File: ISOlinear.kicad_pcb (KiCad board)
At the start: 2 copper layers, 20.3 x 50.8 mm, 23 parts, among them J1 USB_C_Receptacle_USB2.0, J2 Conn_01x20, J3 Conn_01x20, U1 STM32F072CBT6, U2 PRTR5V0U2X, U3 XC6206PxxxMR-Regulator_Linear

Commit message: 1/21
Initial schematic/pcb setup, no routing and no global labels connected
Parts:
- removed J2, J3: Conn_01x20, Connector_PinHeader_2.54mm:PinHeader_1x20_P2.54mm_Vertical
- added D1: D, Diode_SMD:D_SOD-123, B.Cu at (95.4, 130.8)
- added D10: D, Diode_SMD:D_SOD-123, B.Cu at (266.9, 130.7)
- added D11: D, Diode_SMD:D_SOD-123, B.Cu at (285.9, 130.7)
- added D12: D, Diode_SMD:D_SOD-123, B.Cu at (305.0, 130.7)
- added D13: D, Diode_SMD:D_SOD-123, B.Cu at (331.2, 140.3)
- added D14: D, Diode_SMD:D_SOD-123, B.Cu at (95.4, 149.8)
- added D15: D, Diode_SMD:D_SOD-123, B.Cu at (114.5, 149.8)
- added D16: D, Diode_SMD:D_SOD-123, B.Cu at (133.5, 149.8)
- added D17: D, Diode_SMD:D_SOD-123, B.Cu at (152.6, 149.8)
- added D18: D, Diode_SMD:D_SOD-123, B.Cu at (171.6, 149.8)
- added D19: D, Diode_SMD:D_SOD-123, B.Cu at (190.7, 149.8)
- added D2: D, Diode_SMD:D_SOD-123, B.Cu at (114.5, 130.8)
- added D20: D, Diode_SMD:D_SOD-123, B.Cu at (209.7, 149.8)
- added D21: D, Diode_SMD:D_SOD-123, B.Cu at (228.8, 149.8)
- added D22: D, Diode_SMD:D_SOD-123, B.Cu at (247.8, 149.8)
- added D23: D, Diode_SMD:D_SOD-123, B.Cu at (266.9, 149.8)
- added D24: D, Diode_SMD:D_SOD-123, B.Cu at (285.9, 149.8)
- added D25: D, Diode_SMD:D_SOD-123, B.Cu at (307.3, 149.9)
- added D26: D, Diode_SMD:D_SOD-123, B.Cu at (95.4, 168.8)
- added D27: D, Diode_SMD:D_SOD-123, B.Cu at (114.5, 168.9)
- added D28: D, Diode_SMD:D_SOD-123, B.Cu at (133.5, 168.9)
- added D29: D, Diode_SMD:D_SOD-123, B.Cu at (152.6, 168.9)
- added D3: D, Diode_SMD:D_SOD-123, B.Cu at (133.5, 130.8)
- added D30: D, Diode_SMD:D_SOD-123, B.Cu at (171.6, 168.8)
- added D31: D, Diode_SMD:D_SOD-123, B.Cu at (190.7, 168.9)
- added D32: D, Diode_SMD:D_SOD-123, B.Cu at (209.7, 168.9)
- added D33: D, Diode_SMD:D_SOD-123, B.Cu at (228.8, 168.9)
- added D34: D, Diode_SMD:D_SOD-123, B.Cu at (247.8, 169.0)
- added D35: D, Diode_SMD:D_SOD-123, B.Cu at (266.9, 168.8)
- added D36: D, Diode_SMD:D_SOD-123, B.Cu at (285.9, 168.9)
- added D37: D, Diode_SMD:D_SOD-123, B.Cu at (316.9, 168.9)
- added D38: D, Diode_SMD:D_SOD-123, B.Cu at (97.8, 187.9)
- added D39: D, Diode_SMD:D_SOD-123, B.Cu at (121.6, 187.9)
- added D4: D, Diode_SMD:D_SOD-123, B.Cu at (152.6, 130.8)
- added D40: D, Diode_SMD:D_SOD-123, B.Cu at (145.4, 187.9)
- added D41: D, Diode_SMD:D_SOD-123, B.Cu at (178.8, 187.9)
- added D42: D, Diode_SMD:D_SOD-123, B.Cu at (219.2, 187.9)
- added D43: D, Diode_SMD:D_SOD-123, B.Cu at (250.2, 187.9)
- added D44: D, Diode_SMD:D_SOD-123, B.Cu at (271.6, 187.9)
- added D45: D, Diode_SMD:D_SOD-123, B.Cu at (290.7, 187.9)
- added D46: D, Diode_SMD:D_SOD-123, B.Cu at (309.7, 187.9)
- added D47: D, Diode_SMD:D_SOD-123, B.Cu at (328.8, 187.9)
- added D5: D, Diode_SMD:D_SOD-123, B.Cu at (171.6, 130.8)
- added D6: D, Diode_SMD:D_SOD-123, B.Cu at (190.7, 130.8)
- added D7: D, Diode_SMD:D_SOD-123, B.Cu at (209.7, 130.8)
- added D8: D, Diode_SMD:D_SOD-123, B.Cu at (228.8, 130.8)
- added D9: D, Diode_SMD:D_SOD-123, B.Cu at (247.8, 130.7)
- added SW1: SW_PUSH, emptystring:MXOnly-1U-Hotswap, F.Cu at (100.5, 126.8)
- added SW10: SW_PUSH, emptystring:MXOnly-1U-Hotswap, F.Cu at (271.9, 126.8)
- added SW11: SW_PUSH, emptystring:MXOnly-1U-Hotswap, F.Cu at (291.0, 126.8)
- added SW12: SW_PUSH, emptystring:MXOnly-1U-Hotswap, F.Cu at (310.0, 126.8)
- added SW13: SW_PUSH, emptystring:MXOnly-1U-Hotswap, F.Cu at (336.2, 136.3)
- added SW14: SW_PUSH, emptystring:MXOnly-1U-Hotswap, F.Cu at (100.5, 145.9)
- added SW15: SW_PUSH, emptystring:MXOnly-1U-Hotswap, F.Cu at (119.5, 145.9)
- added SW16: SW_PUSH, emptystring:MXOnly-1U-Hotswap, F.Cu at (138.6, 145.9)
- added SW17: SW_PUSH, emptystring:MXOnly-1U-Hotswap, F.Cu at (157.6, 145.9)
- added SW18: SW_PUSH, emptystring:MXOnly-1U-Hotswap, F.Cu at (176.7, 145.9)
- added SW19: SW_PUSH, emptystring:MXOnly-1U-Hotswap, F.Cu at (195.7, 145.9)
- added SW2: SW_PUSH, emptystring:MXOnly-1U-Hotswap, F.Cu at (119.5, 126.8)
- added SW20: SW_PUSH, emptystring:MXOnly-1U-Hotswap, F.Cu at (214.8, 145.9)
- added SW21: SW_PUSH, emptystring:MXOnly-1U-Hotswap, F.Cu at (233.8, 145.9)
- added SW22: SW_PUSH, emptystring:MXOnly-1U-Hotswap, F.Cu at (252.9, 145.9)
- added SW23: SW_PUSH, emptystring:MXOnly-1U-Hotswap, F.Cu at (271.9, 145.9)
- added SW24: SW_PUSH, emptystring:MXOnly-1U-Hotswap, F.Cu at (291.0, 145.9)
- added SW25: SW_PUSH, emptystring:MXOnly-1U-Hotswap, F.Cu at (312.4, 145.9)
- added SW26: SW_PUSH, emptystring:MXOnly-1U-Hotswap, F.Cu at (100.5, 164.9)
- added SW27: SW_PUSH, emptystring:MXOnly-1U-Hotswap, F.Cu at (119.5, 164.9)
- added SW28: SW_PUSH, emptystring:MXOnly-1U-Hotswap, F.Cu at (138.6, 164.9)
- added SW29: SW_PUSH, emptystring:MXOnly-1U-Hotswap, F.Cu at (157.6, 164.9)
- added SW3: SW_PUSH, emptystring:MXOnly-1U-Hotswap, F.Cu at (138.6, 126.8)
- added SW30: SW_PUSH, emptystring:MXOnly-1U-Hotswap, F.Cu at (176.7, 164.9)
- added SW31: SW_PUSH, emptystring:MXOnly-1U-Hotswap, F.Cu at (195.7, 164.9)
- added SW32: SW_PUSH, emptystring:MXOnly-1U-Hotswap, F.Cu at (214.8, 164.9)
- added SW33: SW_PUSH, emptystring:MXOnly-1U-Hotswap, F.Cu at (233.8, 164.9)
- added SW34: SW_PUSH, emptystring:MXOnly-1U-Hotswap, F.Cu at (252.9, 164.9)
- added SW35: SW_PUSH, emptystring:MXOnly-1U-Hotswap, F.Cu at (271.9, 164.9)
- added SW36: SW_PUSH, emptystring:MXOnly-1U-Hotswap, F.Cu at (291.0, 164.9)
- added SW37: SW_PUSH, emptystring:MXOnly-1U-Hotswap, F.Cu at (321.9, 164.9)
- added SW38: SW_PUSH, emptystring:MXOnly-1U-Hotswap, F.Cu at (102.9, 184.0)
- added SW39: SW_PUSH, emptystring:MXOnly-1U-Hotswap, F.Cu at (126.7, 184.0)
- added SW4: SW_PUSH, emptystring:MXOnly-1U-Hotswap, F.Cu at (157.6, 126.8)
- added SW40: SW_PUSH, emptystring:MXOnly-1U-Hotswap, F.Cu at (150.5, 184.0)
- added SW41: SW_PUSH, emptystring:MXOnly-1U-Hotswap, F.Cu at (183.8, 184.0)
- added SW42: SW_PUSH, emptystring:MXOnly-1U-Hotswap, F.Cu at (224.3, 184.0)
- added SW43: SW_PUSH, emptystring:MXOnly-1U-Hotswap, F.Cu at (255.3, 184.0)
- added SW44: SW_PUSH, emptystring:MXOnly-1U-Hotswap, F.Cu at (276.7, 184.0)
- added SW45: SW_PUSH, emptystring:MXOnly-1U-Hotswap, F.Cu at (295.8, 184.0)
- added SW46: SW_PUSH, emptystring:MXOnly-1U-Hotswap, F.Cu at (314.8, 184.0)
- added SW47: SW_PUSH, emptystring:MXOnly-1U-Hotswap, F.Cu at (333.9, 184.0)
- added SW5: SW_PUSH, emptystring:MXOnly-1U-Hotswap, F.Cu at (176.7, 126.8)
- added SW6: SW_PUSH, emptystring:MXOnly-1U-Hotswap, F.Cu at (195.7, 126.8)
- added SW7: SW_PUSH, emptystring:MXOnly-1U-Hotswap, F.Cu at (214.8, 126.8)
- added SW8: SW_PUSH, emptystring:MXOnly-1U-Hotswap, F.Cu at (233.8, 126.8)
- added SW9: SW_PUSH, emptystring:MXOnly-1U-Hotswap, F.Cu at (252.9, 126.8)
- BOOT1, C1, C10, C2, C3, C4, C5, C6, C7, C8, C9, F1, J1, R1, R2, R3, R4, RST1, U1, U2, U3: moved to B.Cu
- moved C4 82.4 mm to (79.3, 142.9)
- moved RST1 80.2 mm to (80.8, 164.2)
- moved C1 78.1 mm to (82.3, 154.9), turned to 180 degrees
- moved C7 78.1 mm to (82.3, 153.6), turned to 0 degrees
- moved R4 77.7 mm to (82.5, 157.2), turned to 180 degrees
- moved F1 76.0 mm to (83.8, 133.7), turned to 0 degrees
- moved J1 76.0 mm to (83.8, 121.4), turned to 0 degrees
- moved U1 76.0 mm to (83.8, 147.2)
- moved U2 76.0 mm to (83.8, 129.4), turned to 0 degrees
- moved R3 74.3 mm to (85.0, 157.2), turned to 180 degrees
- moved C9 73.9 mm to (85.3, 135.9)
- moved C10 72.3 mm to (86.5, 139.4), turned to 180 degrees
- moved BOOT1 72.0 mm to (86.8, 164.2)
- moved C8 72.0 mm to (86.8, 132.7)
- moved R1 72.0 mm to (86.8, 130.7), turned to 180 degrees
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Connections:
- U2 pad 2: D_N -> D-
- U2 pad 3: D_P -> D+
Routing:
- net NRST: track 56.2 -> 19.5 mm
- net /A10: track 26.3 -> 0.00 mm
- net /A9: track 23.5 -> 0.00 mm
- net D+: track 0.00 -> 22.1 mm
- net D_P: track 22.1 -> 0.00 mm
- net BOOT0: track 47.3 -> 25.6 mm
- net /F1: track 21.0 -> 0.00 mm
- net /A8: track 20.8 -> 0.00 mm
- net /A0: track 20.5 -> 0.00 mm
- net D_N: track 20.5 -> 0.00 mm
- net D-: track 0.00 -> 20.5 mm
- net /F0: track 18.3 -> 0.00 mm
- net /B15: track 18.0 -> 0.00 mm
- net /A1: track 17.8 -> 0.00 mm
- net /A13: track 16.0 -> 0.00 mm
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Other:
- board size 20.3 x 50.8 mm -> 268.3 x 73.8 mm

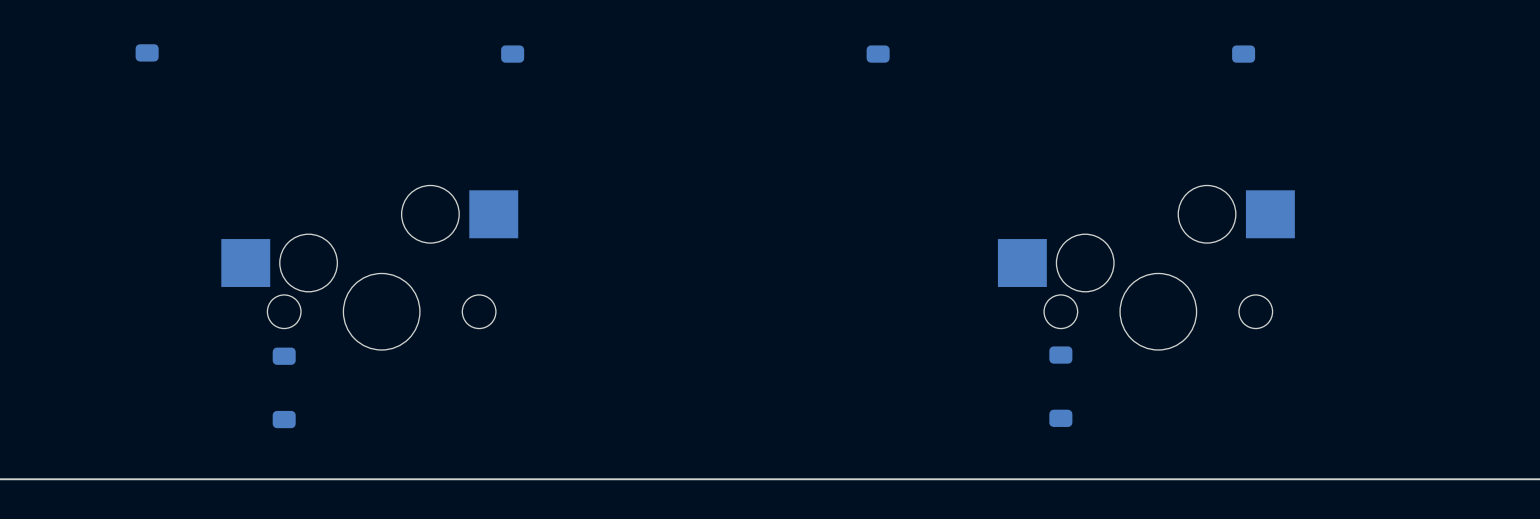
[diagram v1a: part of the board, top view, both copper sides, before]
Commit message: 1/21
Reset grid origin, placed stab footprints
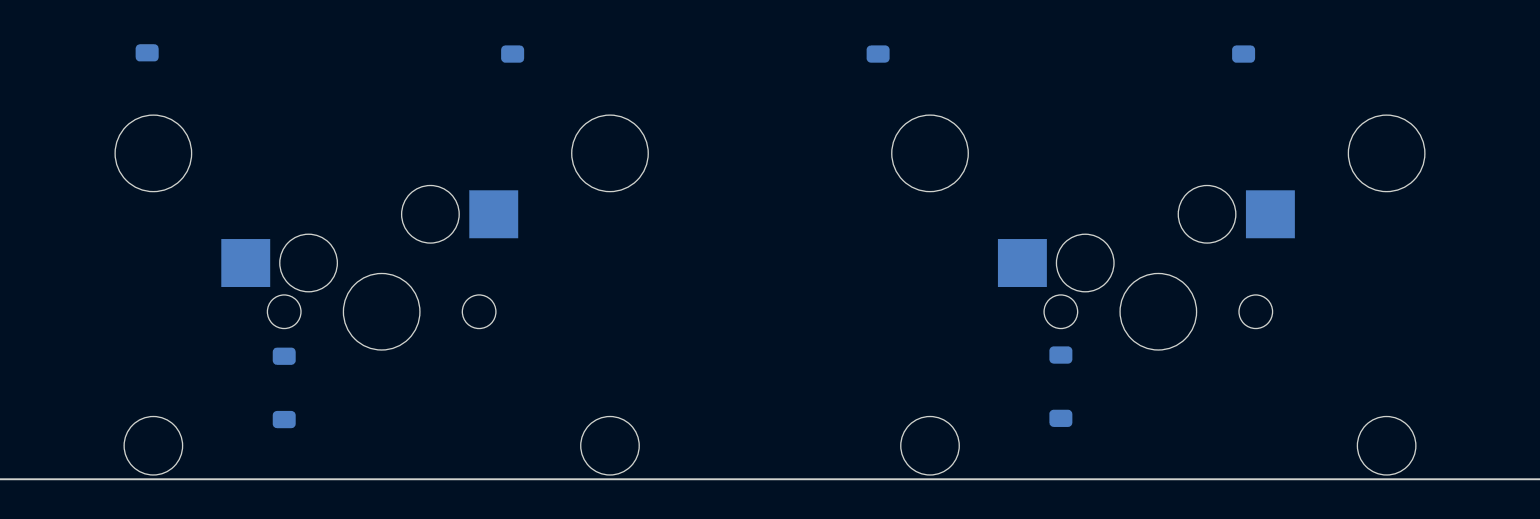
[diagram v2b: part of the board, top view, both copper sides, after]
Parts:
- added REF**: SW_Stabilizer, keyswitches:MX_Stabilizer_2u, F.Cu at (224.3, 184.0)
- added REF**: SW_Stabilizer, keyswitches:MX_Stabilizer_2u, F.Cu at (183.8, 184.0)
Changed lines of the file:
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@@
 		(allow_soldermask_bridges_in_footprints no)
 		(tenting front back)
-		(grid_origin 135.8925 91.9)
+		(grid_origin 90.96625 117.3)
 		(pcbplotparams
 			(layerselection 0x00000000_00000000_55555555_5755f5ff)
@@
 		)
 	)
+	(footprint "keyswitches:MX_Stabilizer_2u"
+		(layer "F.Cu")
+		(at 224.31625 183.975 180)
+		(descr "MX-style stabilizer mount")
+		(tags "MX,cherry,gateron,kailh,pg1511,stabilizer,stab")
+		(property "Reference" "REF**"
+			(at 0 10 0)
+			(layer "Cmts.User")
+			(hide yes)
+			(effects
+				(font
+					(size 1 1)
+					(thickness 0.15)
+				)
+			)
+		)
+		(property "Value" "SW_Stabilizer"
+			(at 0 -8.7 0)
+			(layer "F.Fab")
+			(hide yes)
+			(effects
+				(font
+					(size 1 1)
+					(thickness 0.15)
+				)
+			)
+		)
+		(property "Datasheet" ""
+			(at 0 0 0)
+			(layer "F.Fab")
+			(hide yes)
+			(effects
+				(font
+					(size 1.27 1.27)
+					(thickness 0.15)
+				)
+			)
+		)
+		(property "Description" ""
+			(at 0 0 0)
+			(layer "F.Fab")
+			(hide yes)
+			(effects
+				(font
+					(size 1.27 1.27)
+					(thickness 0.15)
+				)
+			)
+		)
+		(attr through_hole)
+		(fp_circle
+			(center 0 0)
+			(end 3 0)
+			(stroke
+				(width 0.15)
+				(type solid)
+			)
+			(fill no)
+			(layer "Cmts.User")
+		)
+		(pad "" np_thru_hole circle
+			(at -11.9 -6.985 180)
+			(size 3.048 3.048)
+			(drill 3.048)
+			(layers "*.Cu" "*.Mask")
+		)
+		(pad "" np_thru_hole circle
+			(at -11.9 8.255 180)
+			(size 3.9878 3.9878)
+			(drill 3.9878)
+			(layers "*.Cu" "*.Mask")
+		)
+		(pad "" np_thru_hole circle
+			(at 11.9 -6.985 180)
+			(size 3.048 3.048)
+			(drill 3.048)
+			(layers "*.Cu" "*.Mask")
+		)
+		(pad "" np_thru_hole circle
+			(at 11.9 8.255 180)
+			(size 3.9878 3.9878)
+			(drill 3.9878)
+			(layers "*.Cu" "*.Mask")
+		)
+		(embedded_fonts no)
+	)
 	(footprint "emptystring:MXOnly-1U-Hotswap"
 		(layer "F.Cu")
@@
 		)
 	)
+	(footprint "keyswitches:MX_Stabilizer_2u"
+		(layer "F.Cu")
+		(at 183.835 183.975 180)
+		(descr "MX-style stabilizer mount")
+		(tags "MX,cherry,gateron,kailh,pg1511,stabilizer,stab")
+		(property "Reference" "REF**"
+			(at 0 10 0)
+			(layer "Cmts.User")
+			(hide yes)
+			(effects
+				(font
+					(size 1 1)
+					(thickness 0.15)
+				)
+			)
+		)
+		(property "Value" "SW_Stabilizer"
+			(at 0 -8.7 0)
+			(layer "F.Fab")
+			(hide yes)
+			(effects
+				(font
+					(size 1 1)
+					(thickness 0.15)
+				)
+			)
+		)
+		(property "Datasheet" ""
+			(at 0 0 0)
+			(layer "F.Fab")
+			(hide yes)
+			(effects
+				(font
+					(size 1.27 1.27)
+					(thickness 0.15)
+				)
+			)
+		)
+		(property "Description" ""
+			(at 0 0 0)
+			(layer "F.Fab")
+			(hide yes)
+			(effects
+				(font
+					(size 1.27 1.27)
+					(thickness 0.15)
+				)
+			)
+		)
+		(attr through_hole)
+		(fp_circle
+			(center 0 0)
+			(end 3 0)
+			(stroke
+				(width 0.15)
+				(type solid)
+			)
+			(fill no)
+			(layer "Cmts.User")
+		)
+		(pad "" np_thru_hole circle
+			(at -11.9 -6.985 180)
+			(size 3.048 3.048)
+			(drill 3.048)
+			(layers "*.Cu" "*.Mask")
+		)
+		(pad "" np_thru_hole circle
+			(at -11.9 8.255 180)
+			(size 3.9878 3.9878)
+			(drill 3.9878)
+			(layers "*.Cu" "*.Mask")
+		)
+		(pad "" np_thru_hole circle
+			(at 11.9 -6.985 180)
+			(size 3.048 3.048)
+			(drill 3.048)
+			(layers "*.Cu" "*.Mask")
+		)
+		(pad "" np_thru_hole circle
+			(at 11.9 8.255 180)
+			(size 3.9878 3.9878)
+			(drill 3.9878)
+			(layers "*.Cu" "*.Mask")
+		)
+		(embedded_fonts no)
+	)
 	(footprint "emptystring:MXOnly-1U-Hotswap"

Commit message: 1/21
changed layout to teeth version, started routing rows and columns
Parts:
- removed the D13 at (331.2, 140.3)
- removed the D37 at (316.9, 168.9)
- removed D47: D, Diode_SMD:D_SOD-123
- removed the REF** at (224.3, 184.0)
- removed the REF** at (183.8, 184.0)
- removed the SW13 at (336.2, 136.3)
- removed the SW37 at (321.9, 164.9)
- removed SW47: SW_PUSH, emptystring:MXOnly-1U-Hotswap
- added REF**: SW_Stabilizer, keyswitches:MX_Stabilizer_2u, F.Cu at (224.3, 184.1)
- added REF**: SW_Stabilizer, keyswitches:MX_Stabilizer_2u, F.Cu at (183.8, 184.1)
- moved SW24 10.8 mm to (317.1, 155.6)
- moved D24 10.5 mm to (311.6, 159.5)
- moved SW41 7.09 mm to (262.4, 184.1)
- moved D41 6.61 mm to (256.8, 188.1)
- moved SW42 4.71 mm to (281.4, 184.1)
- moved SW44 4.71 mm to (319.5, 184.1)
- moved SW43 4.71 mm to (300.5, 184.1)
- moved D42 4.24 mm to (275.9, 188.2)
- moved D43 4.23 mm to (294.9, 188.1)
- moved D44 4.23 mm to (314.0, 188.1)
- moved SW35 2.33 mm to (293.3, 165.1)
- moved D35 1.86 mm to (287.8, 169.1)
- moved D12 0.58 mm to (304.4, 131.0)
- moved D17 0.58 mm to (171.1, 150.0)
- moved D29 0.58 mm to (171.1, 169.1)
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- renumbered D14 to D13, D15 to D14, D16 to D15, D17 to D16, D18 to D17, D19 to D18, D20 to D19, D21 to D20, D22 to D21, D23 to D22, D24 to D23, D25 to D24, D26 to D25, D27 to D26, D28 to D27, D29 to D28, D30 to D29, D31 to D30, D32 to D31, D33 to D32, D34 to D33, D35 to D34, D36 to D35, D38 to D36, D39 to D37, D40 to D38, D41 to D39, D42 to D40, D43 to D41, D44 to D42, D45 to D43, D46 to D44, SW14 to SW13, SW15 to SW14, SW16 to SW15, SW17 to SW16, SW18 to SW17, SW19 to SW18, SW20 to SW19, SW21 to SW20, SW22 to SW21, SW23 to SW22, SW24 to SW23, SW25 to SW24, SW26 to SW25, SW27 to SW26, SW28 to SW27, SW29 to SW28, SW30 to SW29, SW31 to SW30, SW32 to SW31, SW33 to SW32, SW34 to SW33, SW35 to SW34, SW36 to SW35, SW38 to SW36, SW39 to SW37, SW40 to SW38, SW41 to SW39, SW42 to SW40, SW43 to SW41, SW44 to SW42, SW45 to SW43, SW46 to SW44
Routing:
- net ROW1: track 0.00 -> 220.6 mm
- net ROW3: track 0.00 -> 218.0 mm
- net ROW0: track 0.00 -> 209.5 mm
- net ROW2: track 0.00 -> 192.9 mm
- net Net-(D12-A): track 0.00 -> 5.49 mm
- net Net-(D11-A): track 0.00 -> 5.49 mm
- net Net-(D10-A): track 0.00 -> 5.49 mm
- net Net-(D23-A): track 0.00 -> 5.49 mm
- net Net-(D22-A): track 0.00 -> 5.49 mm
- net Net-(D21-A): track 0.00 -> 5.49 mm
- net Net-(D24-A): track 0.00 -> 5.43 mm
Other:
- board size 268.3 x 73.8 mm -> 253.2 x 73 mm

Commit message: 1/21
Matrix routing done
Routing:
- net COL2: track 0.00 -> 72.7 mm, vias 0 -> 6
- net COL9: track 0.00 -> 70.4 mm, vias 0 -> 6
- net COL6: track 0.00 -> 70.4 mm, vias 0 -> 6
- net COL8: track 0.00 -> 70.3 mm, vias 0 -> 6
- net COL1: track 0.00 -> 68.0 mm, vias 0 -> 6
- net COL4: track 0.00 -> 68.0 mm, vias 0 -> 6
- net COL10: track 0.00 -> 67.1 mm, vias 0 -> 4
- net COL0: track 0.00 -> 64.2 mm, vias 0 -> 6
- net COL11: track 0.00 -> 61.1 mm
- net COL5: track 0.00 -> 42.9 mm, vias 0 -> 4
- net COL7: track 0.00 -> 42.9 mm, vias 0 -> 4
- net COL3: track 0.00 -> 42.8 mm, vias 0 -> 4
- net Net-(D35-A): track 0.00 -> 5.55 mm
- net Net-(D32-A): track 0.00 -> 5.55 mm
- net Net-(D42-A): track 0.00 -> 5.55 mm
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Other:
- outline, holes or cut-outs redrawn

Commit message: 1/22
Routing solutions brainstorm
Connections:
- U1 pad 38: /A15 -> ROW0

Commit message: 1/23
routed and filled tentatively, no grounds on some pins
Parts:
- moved BOOT1 76.5 mm to (135.4, 105.1), turned to 0 degrees
- moved RST1 76.2 mm to (135.4, 111.1), turned to 180 degrees
- moved R3 66.4 mm to (128.4, 106.8), turned to -90 degrees
- moved R4 66.3 mm to (128.4, 109.3), turned to -90 degrees
- moved C1 63.1 mm to (126.1, 109.6), turned to -90 degrees
- moved C7 61.3 mm to (124.9, 109.6), turned to 90 degrees
- moved C6 60.9 mm to (124.1, 104.1), turned to 90 degrees
- moved C5 58.9 mm to (122.6, 103.6), turned to 0 degrees
- moved U1 52.2 mm to (118.4, 108.1), turned to 180 degrees
- moved C3 46.7 mm to (113.9, 103.8), turned to 90 degrees
- moved C4 46.2 mm to (114.1, 112.6), turned to 180 degrees
- moved C2 42.9 mm to (110.9, 102.6), turned to 90 degrees
- moved C10 41.8 mm to (110.6, 105.3), turned to -90 degrees
- moved U3 38.7 mm to (108.1, 103.8), turned to -90 degrees
- moved C9 36.6 mm to (107.1, 106.6), turned to 180 degrees
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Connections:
- U1 pad 12: /A2 -> COL11
- U1 pad 13: /A3 -> COL10
- U1 pad 14: /A4 -> COL9
- U1 pad 15: /A5 -> COL8
- U1 pad 16: /A6 -> COL7
- U1 pad 17: /A7 -> COL6
- U1 pad 18: /B0 -> COL5
- U1 pad 19: /B1 -> COL4
- U1 pad 20: /B2 -> COL3
- U1 pad 21: /B10 -> COL2
- U1 pad 22: /B11 -> COL1
- U1 pad 27: /B14 -> ROW3
- U1 pad 28: /B15 -> ROW2
- U1 pad 29: /A8 -> ROW1
- U1 pad 30: /A9 -> ROW0
- U1 pad 31: /A10 -> COL0
- U1 pad 38: ROW0 -> /A15
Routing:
- net COL11: track 61.1 -> 259.0 mm
- net COL10: track 67.1 -> 247.5 mm
- net COL9: track 70.4 -> 232.9 mm
- net COL8: track 70.3 -> 214.4 mm
- net COL7: track 42.9 -> 168.7 mm
- net COL6: track 70.4 -> 178.1 mm
- net COL5: track 42.9 -> 132.4 mm
- net ROW3: track 218.0 -> 300.2 mm, vias 0 -> 2
- net COL4: track 68.0 -> 139.0 mm
- net ROW2: track 192.9 -> 257.8 mm, vias 0 -> 2
- net COL3: track 42.8 -> 95.5 mm
- net ROW1: track 220.6 -> 267.0 mm, vias 0 -> 2
- net COL2: track 72.7 -> 107.1 mm
- net ROW0: track 209.5 -> 237.6 mm
- net COL0: track 64.2 -> 83.1 mm
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- added copper zone on B.Cu, net (none)
- added copper zone on F.Cu, net (none)
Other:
- board size 253.2 x 73 mm -> 237.3 x 92.9 mm

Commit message: 1/24
updated zones, need to fix footprint and edge cuts around usb
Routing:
- net COL1: track 84.4 -> 83.8 mm
- net GND: vias 8 -> 12
- added copper zone on B.Cu, net GND
- added copper zone on F.Cu, net GND
- removed copper zone on B.Cu, net (none)
- removed copper zone on F.Cu, net (none)
